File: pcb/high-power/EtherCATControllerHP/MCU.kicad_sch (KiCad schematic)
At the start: 8 parts, among them U1 STM32F405RGT6, Y1 ABM3B-8.000MHZ-10-1-U-T

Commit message: starting HP version
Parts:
- removed C50, C51, C52, C53, C54: ${CAPACITANCE}, Capacitor_SMD:C_0603_1608Metric, symbol Device:C
- removed R30: 47K, Resistor_SMD:R_0603_1608Metric, symbol Device:R
- added C13, C33: ${CAPACITANCE}, Capacitor_SMD:C_0402_1005Metric, symbol Device:C
- added C32, C34, C35: ${CAPACITANCE}, Capacitor_SMD:C_0603_1608Metric, symbol Device:C
- added R7: 47K, Resistor_SMD:R_0603_1608Metric, symbol Device:R
- U1: LCSC Part # (none) -> C15742; LCSC Part Number C15742 -> (none)
- Y1: LCSC Part # (none) -> C276420; LCSC Part Number C276420 -> (none)
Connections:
- net VDD is gone; now on net VCC: U1.1 (VBAT), U1.19 (VDD), U1.32 (VDD), U1.48 (VDD), U1.64 (VDD)
- net BOOT0: now also R7.1
- net GND: now also U1.28 (PB2), C13.2, C32.2, C33.2, C34.2, C35.2, R7.2
- net NRST: now also C32.1
- net at U1.47 (VCAP_2): now also C35.1
- net TEMP_MOSFETS: now reaches U1.15 (PA1)
- net TEMP_ICS: now reaches U1.16 (PA2)
- net TEMP_BACKSIDE: now reaches U1.17 (PA3)
- net at U1.31 (VCAP_1): now also C34.1
- net at U1.5 (PH0), Y1.1: now also C13.1
- net at U1.6 (PH1), Y1.3: now also C33.1
- net AVCC renamed VCC
- net M0_ENC_A: no longer names the net of U1.56 (PB4)
- net M0_ENC_B renamed CAN_RX
- net M0_ENC_Z renamed CAN_TX
- net PGOOD: no longer names the net of U1.50 (PA15)
- net USB_DM renamed USB_D-
- net USB_DP renamed USB_D+
- no-connect marks 19 -> 17

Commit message: stash before via stitching
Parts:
- added R10, R19: 22R, Resistor_SMD:R_0402_1005Metric, symbol Device:R
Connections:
- net IRQ: now also U1.42 (PA9); no longer U1.25 (PC5)
- net SPI2_CS: now also U1.43 (PA10); no longer U1.2 (PC13)
- net SPI_CS: now also U1.2 (PC13); no longer U1.41 (PA8)
- net USB_D+: now also R19.2; no longer U1.45 (PA12)
- net USB_D-: now also R10.2; no longer U1.44 (PA11)
- net CAN_MODE: now reaches U1.27 (PB1)
- net BRAKE: no longer names the net of U1.8 (PC0)
- net DIR: no longer names the net of U1.9 (PC1)
- net TEMP_BACKSIDE: no longer names the net of U1.17 (PA3)
- net TEMP_ICS: no longer names the net of U1.16 (PA2)
- new net: R19.1, U1.45 (PA12)
- new net: R10.1, U1.44 (PA11)
- no-connect marks 17 -> 20

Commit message: finished with HP controller
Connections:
- net GND: no longer U1.28 (PB2)
- no-connect marks 20 -> 21
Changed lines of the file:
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@@
+	)
+	(no_connect
+		(at 189.23 100.33)
 	)
 	(no_connect
@@
 	(wire
 		(pts
-			(xy 182.88 100.33) (xy 203.2 100.33)
-		)
-		(stroke
-			(width 0)
-			(type default)
-		)
-	)
-	(wire
-		(pts
 			(xy 147.32 100.33) (xy 132.08 100.33)
 		)
@@
 	(wire
 		(pts
-			(xy 203.2 100.33) (xy 203.2 102.87)
-		)
-		(stroke
-			(width 0)
-			(type default)
-		)
-	)
-	(wire
-		(pts
 			(xy 92.71 109.22) (xy 92.71 111.76)
 		)
@@
 		(pts
 			(xy 133.35 121.92) (xy 133.35 120.65)
+		)
+		(stroke
+			(width 0)
+			(type default)
+		)
+	)
+	(wire
+		(pts
+			(xy 182.88 100.33) (xy 189.23 100.33)
 		)
 		(stroke
@@
 					(unit 1)
 				)
-			)
-		)
-	)
-	(symbol
-		(lib_id "power:GND")
-		(at 203.2 102.87 0)
-		(unit 1)
-		(exclude_from_sim no)
-		(in_bom yes)
-		(on_board yes)
-		(dnp no)
-		(fields_autoplaced yes)
-		(property "Reference" "#PWR037"
-			(at 203.2 109.22 0)
-			(effects
-				(font
-					(size 1.27 1.27)
-				)
-				(hide yes)
-			)
-		)
-		(property "Value" "GND"
-			(at 203.2 107.95 0)
-			(effects
-				(font
-					(size 1.27 1.27)
-				)
-			)
-		)
-		(property "Footprint" ""
-			(at 203.2 102.87 0)
-			(effects
-				(font
-					(size 1.27 1.27)
-				)
-				(hide yes)
-			)
-		)
-		(property "Datasheet" ""
-			(at 203.2 102.87 0)
-			(effects
-				(font
-					(size 1.27 1.27)
-				)
-				(hide yes)
-			)
-		)
-		(property "Description" "Power symbol creates a global label with name \"GND\" , ground"
-			(at 203.2 102.87 0)
-			(effects
-				(font
-					(size 1.27 1.27)
-				)
-				(hide yes)
-			)
-		)
-		(pin "1"
-		)
-		(instances
-			(project "EtherCATSTM32"
-				(path "/4c927f80-855d-490a-80b2-e5c55283621a/5ac89ae2-4d69-4fd6-b754-7aee59ff7a56"
-					(reference "#PWR037")
-					(unit 1)
-				)

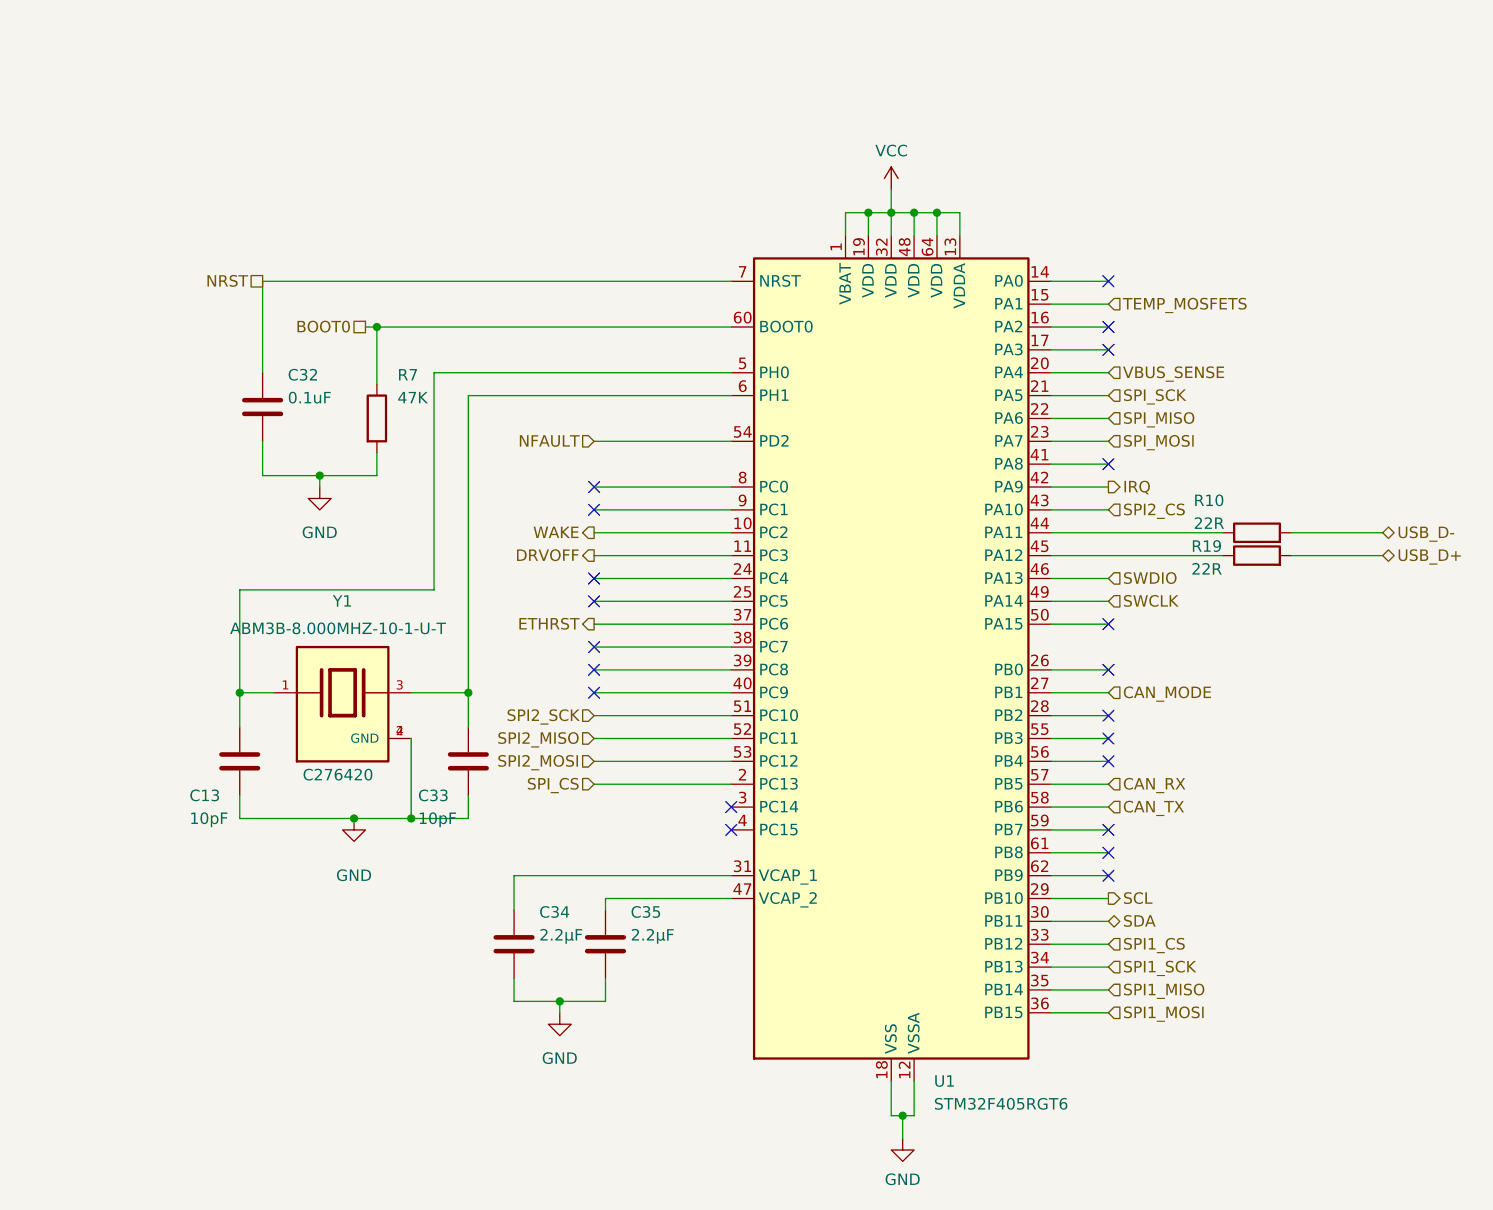
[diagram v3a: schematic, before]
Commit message: redid layout and mounting
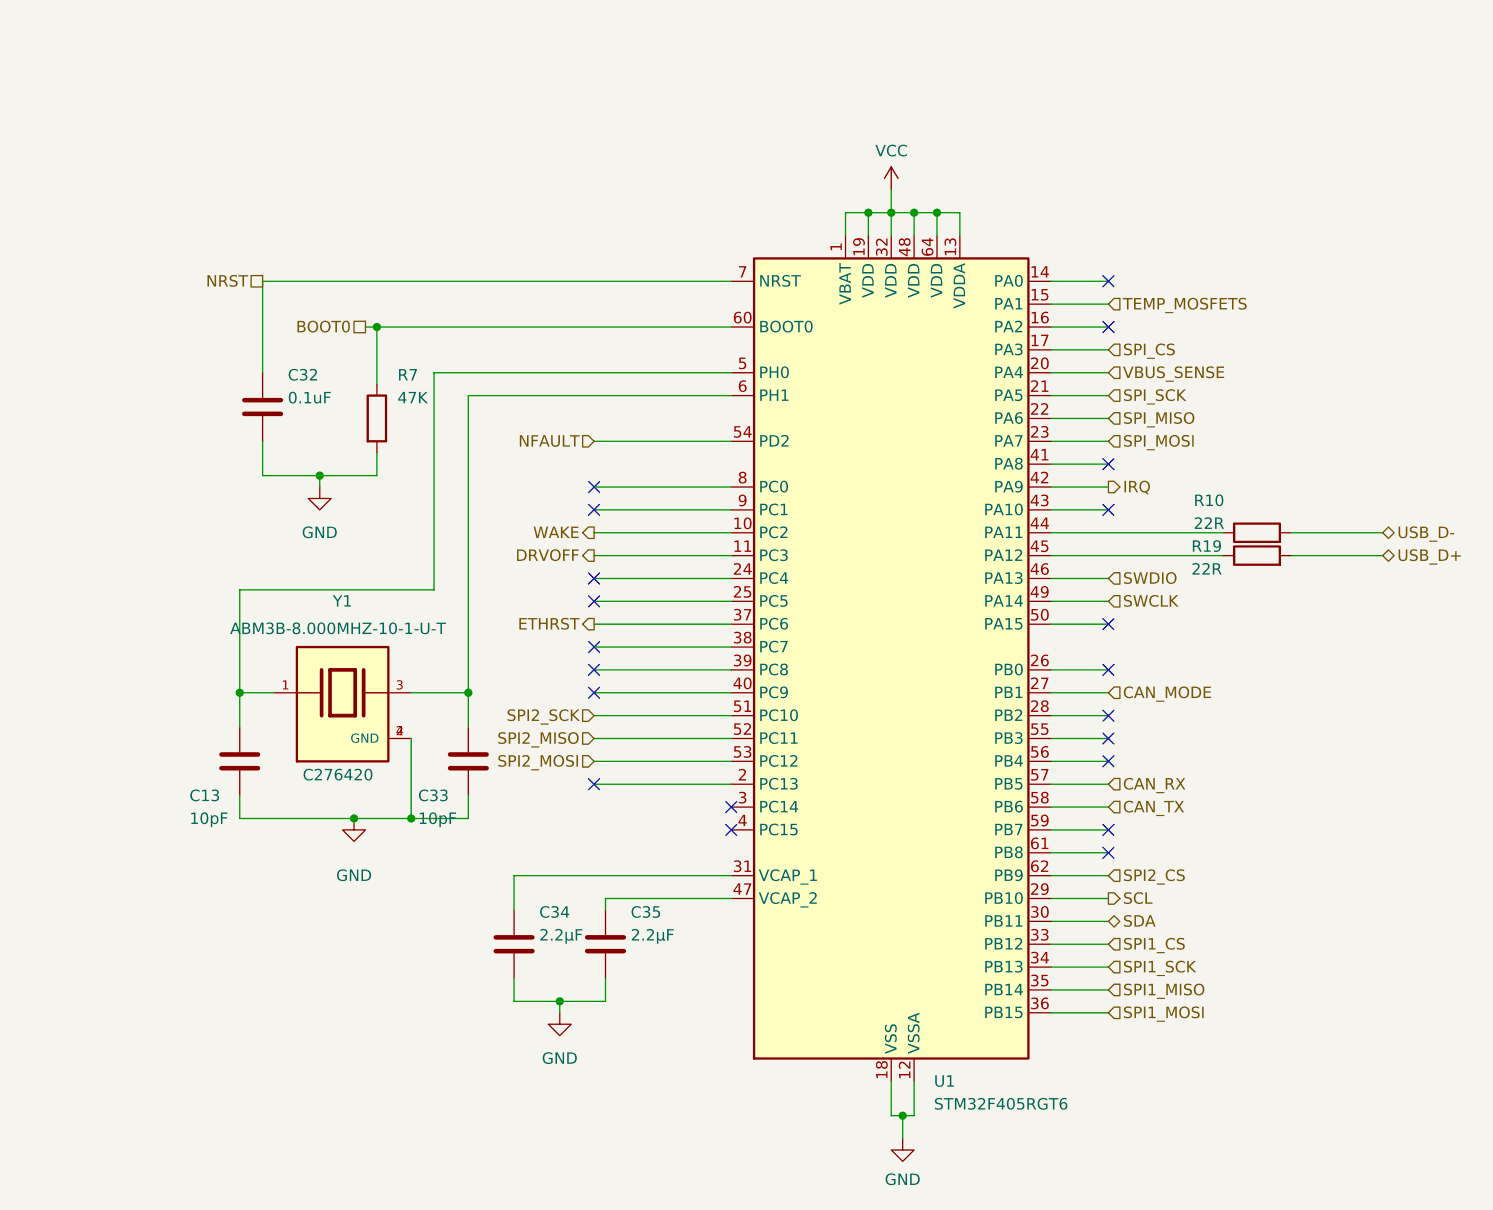
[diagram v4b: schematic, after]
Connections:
- net SPI2_CS: now also U1.62 (PB9); no longer U1.43 (PA10)
- net SPI_CS: now also U1.17 (PA3); no longer U1.2 (PC13)
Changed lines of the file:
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@@
 	)
 	(no_connect
-		(at 189.23 118.11)
+		(at 132.08 107.95)
 	)
 	(no_connect
@@
 	)
 	(no_connect
+		(at 189.23 77.47)
+	)
+	(no_connect
 		(at 147.32 113.03)
 	)
@@
 	(no_connect
 		(at 189.23 115.57)
-	)
-	(no_connect
-		(at 189.23 59.69)
 	)
 	(no_connect
@@
 		)
 	)
-	(hierarchical_label "SPI_CS"
-		(shape input)
-		(at 132.08 107.95 180)
-		(fields_autoplaced yes)
-		(effects
-			(font
-				(size 1.27 1.27)
-			)
-			(justify right)
-		)
-	)
 	(hierarchical_label "SPI_SCK"
 		(shape input)
@@
 		)
 	)
+	(hierarchical_label "SPI_CS"
+		(shape input)
+		(at 189.23 59.69 0)
+		(fields_autoplaced yes)
+		(effects
+			(font
+				(size 1.27 1.27)
+			)
+			(justify left)
+		)
+	)
 	(hierarchical_label "BOOT0"
 		(shape passive)
@@
 		)
 	)
+	(hierarchical_label "SPI2_CS"
+		(shape input)
+		(at 189.23 118.11 0)
+		(fields_autoplaced yes)
+		(effects
+			(font
+				(size 1.27 1.27)
+			)
+			(justify left)
+		)
+	)
 	(hierarchical_label "SPI2_MISO"
 		(shape input)
@@
 		)
 	)
-	(hierarchical_label "SPI2_CS"
-		(shape input)
-		(at 189.23 77.47 0)
-		(fields_autoplaced yes)
-		(effects
-			(font
-				(size 1.27 1.27)
-			)
-			(justify left)
-		)
-	)

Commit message: fixed bom
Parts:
- R10, R19: LCSC Part # C107701 -> C114765
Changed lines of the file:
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@@
 			)
 		)
-		(property "LCSC Part #" "C107701"
+		(property "LCSC Part #" "C114765"
 			(at 205.74 82.55 0)
 			(effects
@@
 			)
 		)
-		(property "LCSC Part #" "C107701"
+		(property "LCSC Part #" "C114765"
 			(at 205.74 80.01 0)
 			(effects
